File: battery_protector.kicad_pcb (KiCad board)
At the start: 4 copper layers, 85.7 x 65.3 mm, 111 parts, among them J1 TB005-762-02BE, J2 TB005-762-02BE, J3 USB_C_Receptacle_USB2.0_16P, J5 Conn_01x12, Q1 SQJQ184ER, Q2 SQJQ184ER, Q3 SQJQ184ER, Q4 SQJQ184ER, Q5 MMBT3904, Q6 MMBT3904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

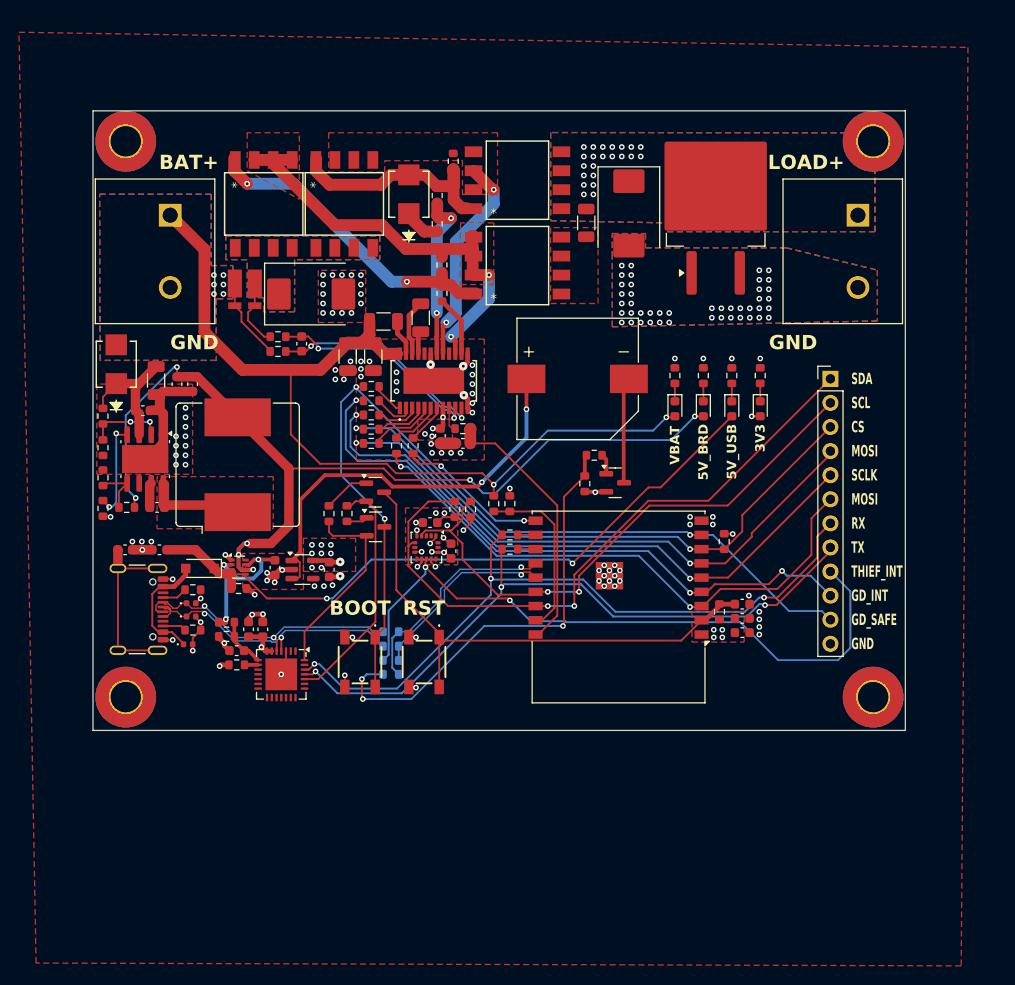
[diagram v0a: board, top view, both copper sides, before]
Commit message: Caught some issues and made final changes for manufacturing (#9)
Caught some issues and made final changes for manufacturing including correcting the imu and J2 footprints, updating the clearance rules we imported from pcbway (.09mm->0.1mm), and the addition of stitching capacitors for usb signal.
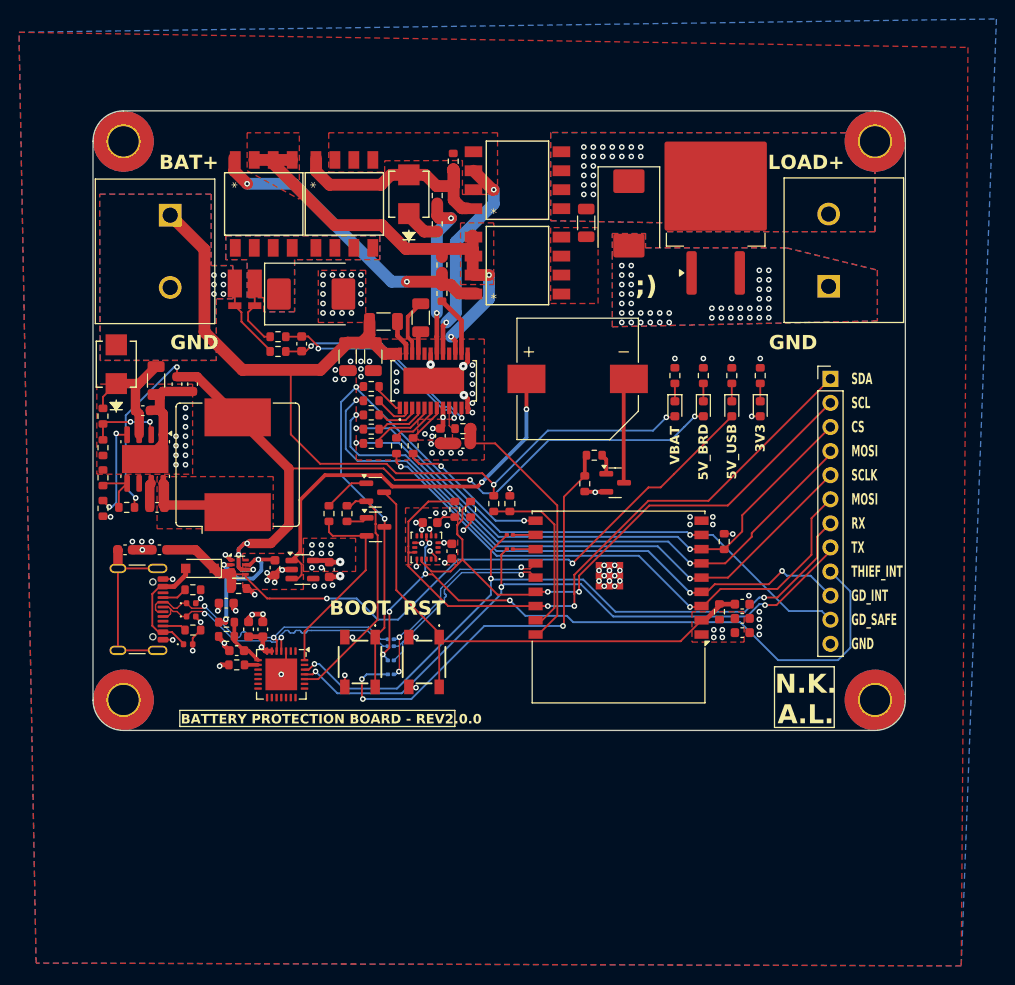
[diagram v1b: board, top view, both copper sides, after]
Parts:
- added C25: 0.1u, Capacitor_SMD:C_0603_1608Metric, F.Cu at (91.8, 114.6)
- R32, R33, R44, R45, R46, R9: footprint Resistor_SMD:R_0603_1608Metric -> Resistor_SMD:R_0201_0603Metric
- U6: value LIS3DH -> LIS3DHTR; footprint Package_LGA:LGA-16_3x3mm_P0.5mm_LayoutBorder3x5y -> custom_footprints:LGA-16_3x3mm_P0.5mm_LayoutBorder3x5y_2
- moved J2 8.11 mm to (155.3, 81.2), turned to 90 degrees
- moved R44 0.79 mm to (109.2, 118.4)
- moved H5 0.38 mm to (81.0, 124.8)
- moved H8 0.36 mm to (160.2, 124.8)
- moved H6 0.24 mm to (81.0, 65.9)
- moved H7 0.20 mm to (160.2, 65.9)
- moved C16 0.08 mm to (115.6, 109.1), turned to -90 degrees
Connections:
- J2 pad 1: LOAD+ -> GND
- J2 pad 2: GND -> LOAD+
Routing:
- net /MCU/THIEF_INT: track 70.9 -> 73.5 mm, vias 2 -> 5
- net +5V0_USB: track 72.3 -> 74.1 mm
- net /DC-DC/USB_DN: track 29.8 -> 31.4 mm
- net /MCU/DP: track 20.2 -> 21.7 mm
- net /MCU/I2C1_SCL: track 60.7 -> 62.2 mm
- net +3V3: track 21.5 -> 22.2 mm
- net Net-(U5-IO21/TXD): track 1.88 -> 2.39 mm
- net Net-(U5-IO20/RXD): track 1.88 -> 2.39 mm
- net /MCU/BEEP_BEEP_BITCH: track 47.9 -> 48.4 mm
- net GND: track 67.8 -> 68.2 mm, vias 155 -> 156
- net /MCU/DN: track 23.3 -> 23.4 mm, vias 1 -> 3
- removed copper zone on In2.Cu, net GND
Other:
- outline, holes or cut-outs redrawn
- board text added: ";)"
- board text added: "BATTERY PROTECTION BOARD - REV2.0.0"
- board text added: "N.K. A.L."
